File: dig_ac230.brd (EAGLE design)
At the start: 100 x 85 mm, 134 parts, among them IC1 74HC595D, IC101 ATMEGA32A-AU, IC102 DS1337S, IC103 MAX487CSA, IC104 74HC166D, IC2 LTV-356T, IC3 LTV-356T, IC4 LTV-356T, IC5 LTV-356T, IC6 LTV-356T, IC7 LTV-356T, IC8 LTV-356T, IC9 LTV-356T, K301 S202S02, K302 S202S02, K303 S202S02, K304 S202S02, K305 S202S02, K306 S202S02, K307 S202S02, K308 S202S02, Q1 32,768kHz, Q2 BCR191, Q3 BCR191, Q4 BCR191, Q5 BCR191, Q6 BCR191, Q7 BCR191, Q8 BCR191, Q9 BCR191, X1 RIA-73-02, X10 RIA-73-02, X11 RIA-73-02, X12 RIA-73-02, X2 RIA-73-02, X3 RIA-73-02, X4 RIA-73-02, X5 RIA-73-02, X6 RIA-73-02, X7 RIA-73-02, X8 RIA-73-02, X9 RIA-73-02

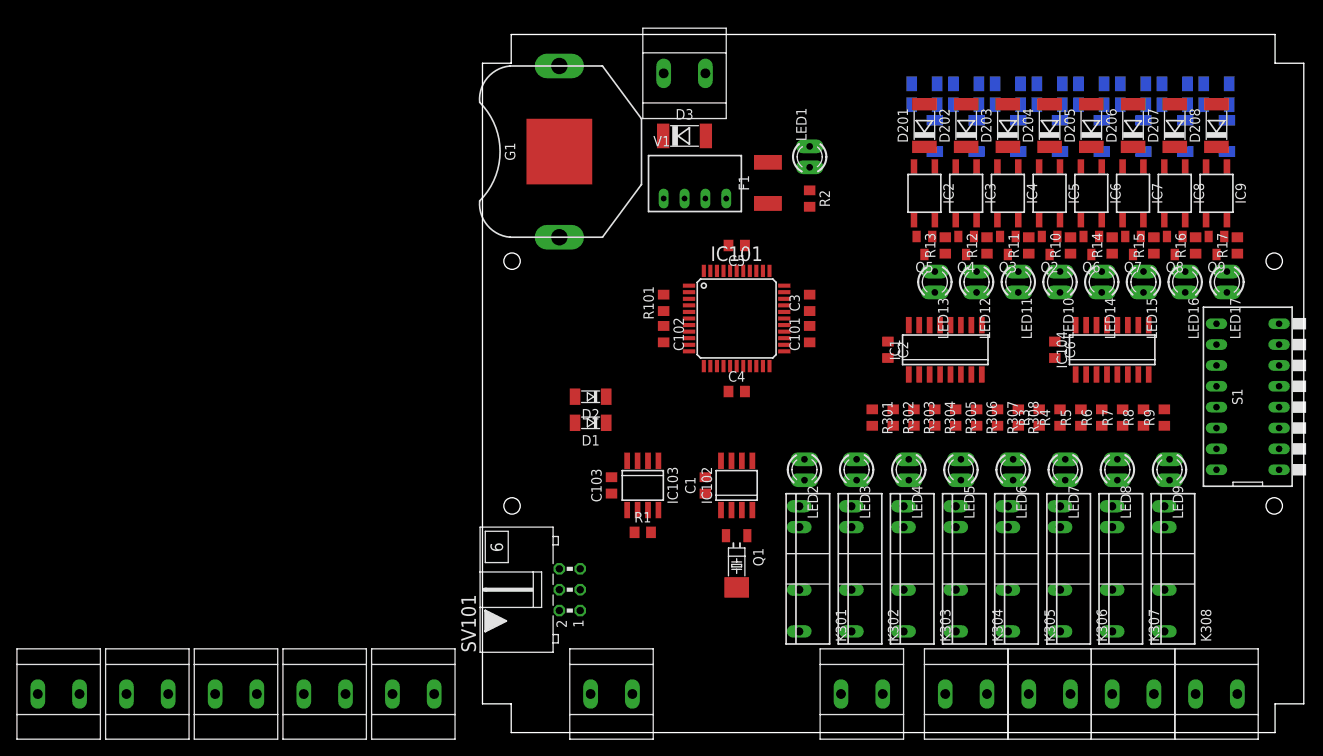
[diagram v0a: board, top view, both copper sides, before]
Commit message: Bauteile neu positoniert
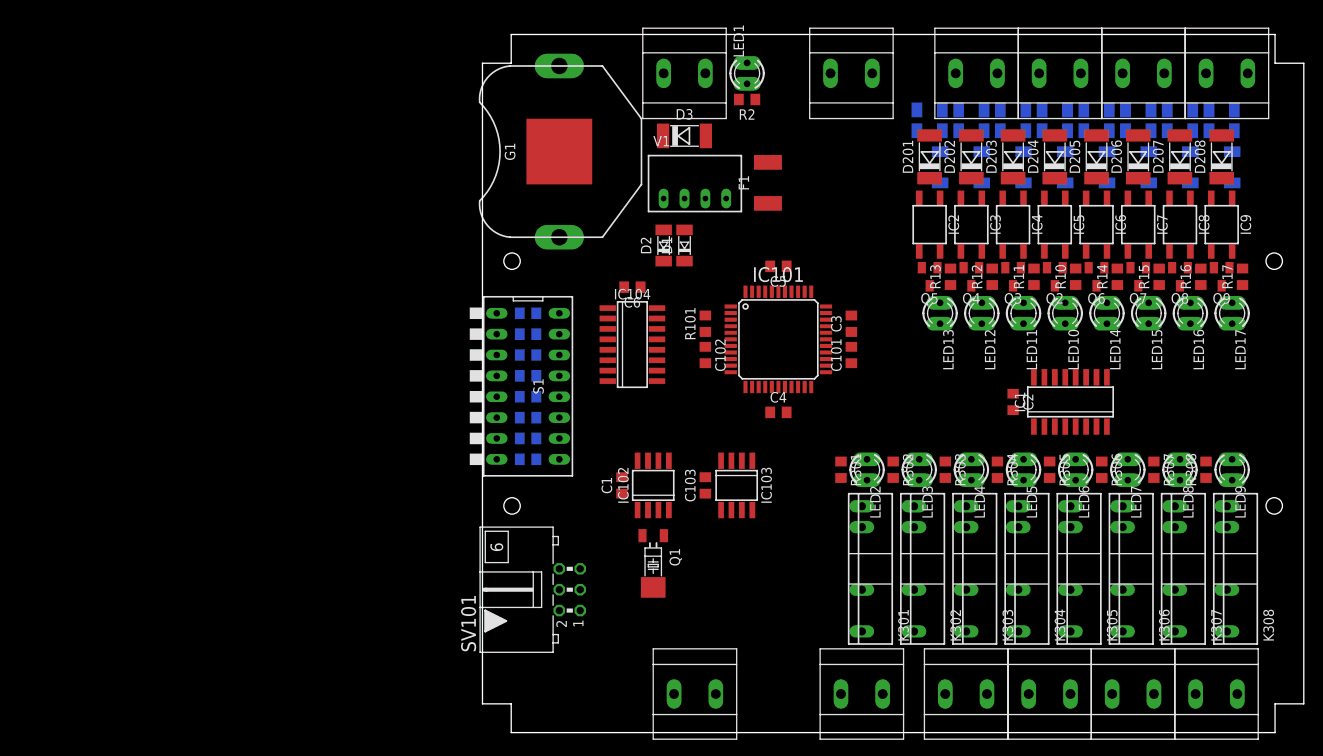
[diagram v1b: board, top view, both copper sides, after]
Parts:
- moved X6 151.6 mm to (92.7, 80.6), turned to 180 degrees
- moved X5 133.9 mm to (82.5, 80.6), turned to 180 degrees
- moved X7 122.6 mm to (47.0, 80.6), turned to 180 degrees
- moved X4 117.2 mm to (72.4, 80.6), turned to 180 degrees
- moved X3 102.0 mm to (62.2, 80.6), turned to 180 degrees
- moved S1 87.6 mm to (7.62, 42.5), turned to 270 degrees
- moved R9 77.5 mm to (7.62, 36.2), flipped to the bottom, turned to 180 degrees
- moved R8 74.9 mm to (7.62, 38.7), flipped to the bottom, turned to 180 degrees
- moved R7 72.4 mm to (7.62, 41.3), flipped to the bottom, turned to 180 degrees
- moved R6 70.0 mm to (7.62, 43.8), flipped to the bottom, turned to 180 degrees
- moved R5 67.7 mm to (7.62, 46.4), flipped to the bottom, turned to 180 degrees
- moved R4 65.6 mm to (7.62, 48.9), flipped to the bottom, turned to 180 degrees
- moved R3 63.5 mm to (7.62, 51.4), flipped to the bottom, turned to 180 degrees
- moved IC104 58.4 mm to (20.3, 47.6), turned to 270 degrees
- moved C6 52.0 mm to (20.3, 54.6), turned to 180 degrees
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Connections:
- net GNDIO renamed N
- net N$90 renamed L
- net +5V: now also S1.14, S1.24, S1.34, S1.44, S1.54, S1.64, S1.74; no longer S1.13, S1.23, S1.33, S1.43, S1.53, S1.63, S1.73
- net N$20: now also X2.1; no longer X2.2
- net N$22: now also X2.2; no longer X2.1
- net N$26: now also S1.13; no longer S1.14
- net N$27: now also S1.23; no longer S1.24
- net N$28: now also S1.33; no longer S1.34
- net N$29: now also S1.43; no longer S1.44
- net N$30: now also S1.53; no longer S1.54
- net N$31: now also S1.63; no longer S1.64
- net N$32: now also S1.73; no longer S1.74

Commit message: rev1 geroutet
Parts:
- moved IC103 11.4 mm to (21.6, 29.8)
- moved C103 11.4 mm to (17.8, 29.8), turned to 270 degrees
- moved C1 9.55 mm to (28.6, 29.8), turned to 270 degrees
- moved IC102 9.55 mm to (32.4, 29.8)
- moved Q1 9.55 mm to (32.4, 22.2)
- moved R101 5.85 mm to (24.8, 54.0)
- moved D1 4.84 mm to (31.1, 61.6), turned to 0 degrees
- moved C3 3.70 mm to (50.2, 48.3), turned to 270 degrees
- moved C102 2.69 mm to (27.3, 48.3)
- moved C101 2.01 mm to (46.4, 48.3)
- moved D2 2.01 mm to (24.8, 61.6), turned to 180 degrees
- moved C4 1.42 mm to (36.8, 38.7)
- moved C5 1.42 mm to (36.8, 57.8)
- moved IC101 1.27 mm to (36.8, 48.3)
- moved C6 1.27 mm to (19.1, 54.6)
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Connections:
- net N$20: now also S1.84; no longer R1.1
- net N$22: now also R1.1; no longer S1.84
- net RE: now also IC101.14; no longer IC101.13
- net TE: now also IC101.13; no longer IC101.14
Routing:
- net +5V: track 0.00 -> 278.5 mm, vias 0 -> 23
- net L: track 0.00 -> 133.7 mm
- net GND: track 0.00 -> 114.4 mm, vias 0 -> 18
- net C1: track 0.00 -> 79.3 mm, vias 0 -> 3
- net C2: track 0.00 -> 67.6 mm, vias 0 -> 4
- net !R: track 0.00 -> 67.0 mm, vias 0 -> 3
- net IN7: track 0.00 -> 65.6 mm, vias 0 -> 2
- net N: track 0.00 -> 64.7 mm
- net IN6: track 0.00 -> 60.2 mm, vias 0 -> 2
- net VCC: track 0.00 -> 58.6 mm, vias 0 -> 4
- net MISO: track 0.00 -> 56.8 mm, vias 0 -> 2
- net IN5: track 0.00 -> 54.8 mm, vias 0 -> 2
- net MOSI: track 0.00 -> 54.7 mm, vias 0 -> 2
- net SCK: track 0.00 -> 52.3 mm, vias 0 -> 2
- net N$42: track 0.00 -> 49.5 mm, vias 0 -> 2
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- added copper zone on layer 1, net +5V
- added copper zone on layer 16, net GND

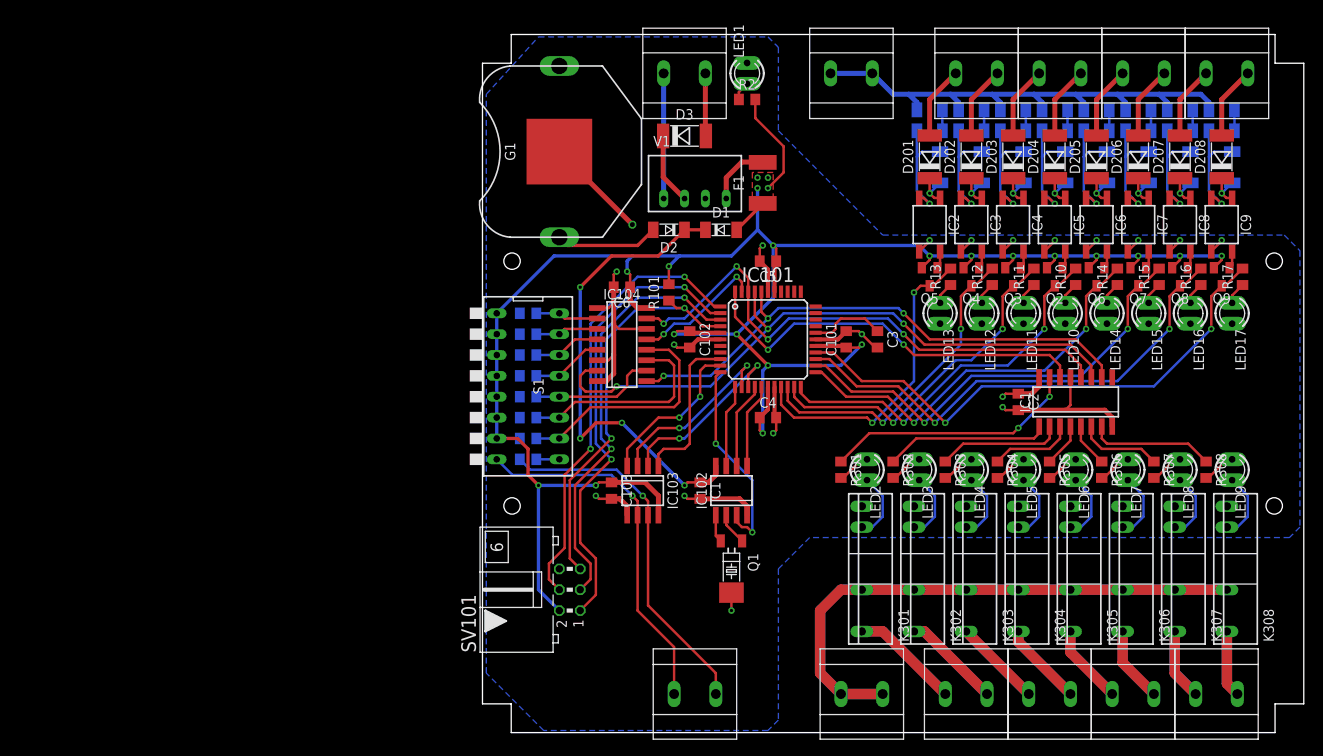
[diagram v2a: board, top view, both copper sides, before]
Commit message: kleinere Designfehler beseitigt
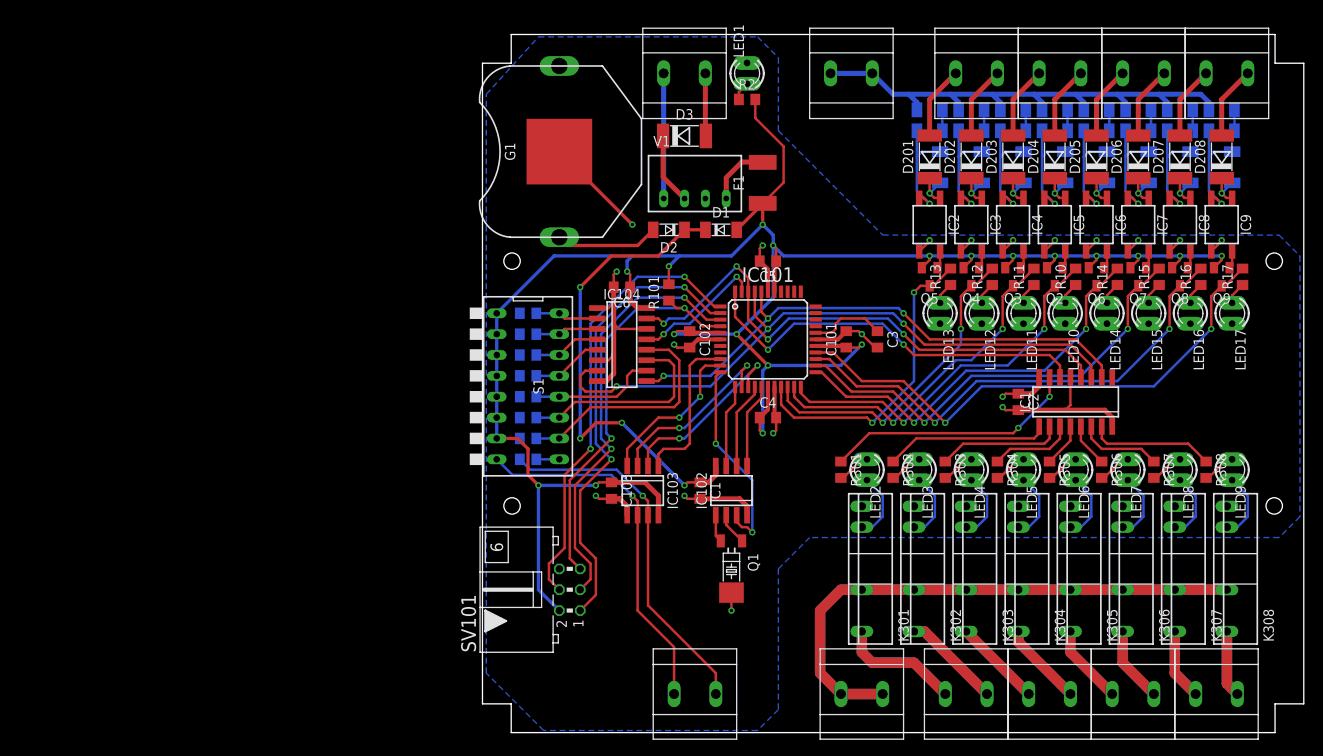
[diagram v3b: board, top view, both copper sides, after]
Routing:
- net N$68: track 26.6 -> 29.6 mm
- net +5V: track 278.5 -> 279.3 mm, vias 23 -> 20
- removed copper zone on layer 1, net +5V
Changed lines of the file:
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@@
 <hole x="5.6701" y="27.981" drill="2"/>
 <hole x="5.6701" y="57.781" drill="2"/>
-<polygon width="0" layer="40">
-<vertex x="2.0701" y="85.381"/>
-<vertex x="2.0701" y="0.381"/>
-<vertex x="8.0701" y="0.381"/>
-<vertex x="8.0701" y="85.381"/>
-</polygon>
-<polygon width="0" layer="40">
-<vertex x="96.0701" y="0.381"/>
-<vertex x="96.0701" y="85.381"/>
-<vertex x="102.0701" y="85.381"/>
-<vertex x="102.0701" y="0.381"/>
-</polygon>
-<polygon width="0" layer="40">
-<vertex x="2.0701" y="0.381"/>
-<vertex x="2.0701" y="3.381"/>
-<vertex x="101.4351" y="3.381"/>
-<vertex x="102.0701" y="0.381"/>
-</polygon>
-<polygon width="0" layer="40">
-<vertex x="2.0701" y="85.381"/>
-<vertex x="2.0701" y="82.381"/>
-<vertex x="102.0701" y="82.381"/>
-<vertex x="102.0701" y="85.381"/>
-</polygon>
-<polygon width="0" layer="39">
-<vertex x="4.0701" y="38.881"/>
-<vertex x="4.0701" y="46.881"/>
-<vertex x="2.0701" y="46.881"/>
-<vertex x="2.0701" y="38.881"/>
-</polygon>
-<polygon width="0" layer="39">
-<vertex x="102.0701" y="46.881"/>
-<vertex x="102.0701" y="38.881"/>
-<vertex x="100.0701" y="38.881"/>
-<vertex x="100.0701" y="46.881"/>
-</polygon>
 <circle x="8.8901" y="80.681" radius="1.8" width="0.1" layer="101"/>
 <circle x="13.9701" y="80.681" radius="1.8" width="0.1" layer="101"/>
@@
 <polygon width="0.4064" layer="16">
 <vertex x="8.89" y="85.09"/>
-<vertex x="36.83" y="85.09"/>
-<vertex x="38.1" y="83.82"/>
+<vertex x="35.56" y="85.09"/>
+<vertex x="38.1" y="82.55"/>
 <vertex x="38.1" y="73.66"/>
 <vertex x="50.8" y="60.96"/>
-<vertex x="99.695" y="60.96"/>
-<vertex x="101.6" y="59.055"/>
-<vertex x="101.6" y="25.4"/>
-<vertex x="100.33" y="24.13"/>
+<vertex x="99.06" y="60.96"/>
+<vertex x="101.6" y="58.42"/>
+<vertex x="101.6" y="26.67"/>
+<vertex x="99.06" y="24.13"/>
 <vertex x="41.91" y="24.13"/>
 <vertex x="38.1" y="20.32"/>
-<vertex x="38.1" y="1.905"/>
-<vertex x="36.83" y="0.635"/>
+<vertex x="38.1" y="3.175"/>
+<vertex x="35.56" y="0.635"/>
 <vertex x="9.525" y="0.635"/>
 <vertex x="2.54" y="7.62"/>
@@
 <wire x1="16.05" y1="45.72" x2="17.415" y2="45.72" width="0.3048" layer="1"/>
 <wire x1="17.415" y1="45.72" x2="18.05" y2="46.355" width="0.3048" layer="1"/>
-<wire x1="11.43" y1="71.12" x2="20.32" y2="62.23" width="0.6096" layer="1"/>
-<via x="20.32" y="62.23" extent="1-16" drill="0.6"/>
+<wire x1="11.43" y1="71.12" x2="20.32" y2="62.23" width="0.4064" layer="1"/>
+<via x="20.32" y="62.23" extent="1-16" drill="0.4"/>
 <wire x1="42.63" y1="48.26" x2="45.355" y2="48.26" width="0.508" layer="1"/>
 <wire x1="45.355" y1="48.26" x2="46.355" y2="49.26" width="0.508" layer="1"/>
@@
 <wire x1="21.86" y1="30.845" x2="23.495" y2="29.21" width="0.6096" layer="1"/>
 <via x="19.685" y="56.515" extent="1-16" drill="0.4"/>
-<polygon width="0.6096" layer="1">
-<vertex x="37.465" y="64.135"/>
-<vertex x="37.465" y="68.58"/>
-<vertex x="34.925" y="68.58"/>
-<vertex x="34.925" y="64.135"/>
-</polygon>
-<via x="36.83" y="66.675" extent="1-16" drill="0.4"/>
-<via x="35.56" y="66.675" extent="1-16" drill="0.4"/>
-<via x="36.83" y="67.945" extent="1-16" drill="0.4"/>
+<via x="36.195" y="62.23" extent="1-16" drill="0.4"/>
 <wire x1="20.05" y1="54.61" x2="20.05" y2="52.975" width="0.6096" layer="1"/>
 <wire x1="20.05" y1="52.975" x2="20.955" y2="52.07" width="0.6096" layer="1"/>
 <wire x1="20.955" y1="52.07" x2="22.05" y2="52.07" width="0.6096" layer="1"/>
-<via x="35.56" y="67.945" extent="1-16" drill="0.4"/>
 <wire x1="33.015" y1="61.595" x2="33.015" y2="61.63" width="0.6096" layer="1"/>
 <wire x1="35.29" y1="77.47" x2="35.29" y2="75.2" width="0.3048" layer="1"/>
 <wire x1="35.29" y1="75.2" x2="38.735" y2="71.755" width="0.3048" layer="1"/>
-<wire x1="38.735" y1="71.755" x2="38.735" y2="68.58" width="0.3048" layer="1"/>
-<wire x1="38.735" y1="68.58" x2="36.83" y2="66.675" width="0.3048" layer="1"/>
+<wire x1="38.735" y1="71.755" x2="38.735" y2="67.35" width="0.3048" layer="1"/>
 <wire x1="42.63" y1="47.46" x2="46.155" y2="47.46" width="0.508" layer="1"/>
 <wire x1="46.155" y1="47.46" x2="46.355" y2="47.26" width="0.508" layer="1"/>
@@
 <wire x1="3.81" y1="41.275" x2="3.81" y2="38.735" width="0.4064" layer="16"/>
 <wire x1="3.81" y1="38.735" x2="3.81" y2="36.195" width="0.4064" layer="16"/>
-<wire x1="35.56" y1="66.675" x2="35.56" y2="61.595" width="0.4064" layer="16"/>
-<wire x1="35.56" y1="61.595" x2="37.465" y2="59.69" width="0.4064" layer="16"/>
-<wire x1="35.56" y1="61.595" x2="32.385" y2="58.42" width="0.4064" layer="16"/>
+<wire x1="36.195" y1="62.23" x2="32.385" y2="58.42" width="0.4064" layer="16"/>
 <wire x1="32.385" y1="58.42" x2="26.035" y2="58.42" width="0.4064" layer="16"/>
 <wire x1="26.035" y1="58.42" x2="20.32" y2="58.42" width="0.4064" layer="16"/>
@@
 <via x="24.765" y="57.15" extent="1-16" drill="0.4"/>
 <wire x1="24.765" y1="57.15" x2="26.035" y2="58.42" width="0.4064" layer="16"/>
-<wire x1="37.465" y1="59.69" x2="55.245" y2="59.69" width="0.4064" layer="16"/>
-<wire x1="55.245" y1="59.69" x2="56.515" y2="58.42" width="0.4064" layer="16"/>
 <wire x1="37.465" y1="59.69" x2="37.465" y2="53.34" width="0.4064" layer="16"/>
 <wire x1="37.465" y1="53.34" x2="33.02" y2="48.895" width="0.4064" layer="16"/>
@@
 <wire x1="8.89" y1="17.78" x2="8.89" y2="30.48" width="0.4064" layer="16"/>
 <wire x1="36.195" y1="64.775" x2="33.015" y2="61.595" width="0.4064" layer="1"/>
-<wire x1="70.805" y1="56.98" x2="69.85" y2="43.64" width="0" layer="19" extent="1-1"/>
+<wire x1="37.465" y1="59.69" x2="37.465" y2="60.96" width="0.4064" layer="16"/>
+<wire x1="37.465" y1="60.96" x2="36.195" y2="62.23" width="0.4064" layer="16"/>
+<wire x1="56.515" y1="58.42" x2="38.735" y2="58.42" width="0.4064" layer="16"/>
+<wire x1="38.735" y1="58.42" x2="37.465" y2="59.69" width="0.4064" layer="16"/>
+<wire x1="69.85" y1="43.64" x2="70.805" y2="56.98" width="0" layer="19" extent="1-1"/>
+<wire x1="38.735" y1="67.35" x2="36.195" y2="64.81" width="0.3048" layer="1"/>
+<wire x1="36.195" y1="64.775" x2="36.195" y2="62.23" width="0.4064" layer="1"/>
 </signal>
 <signal name="N$42">
@@
 <contactref element="X8" pad="1"/>
 <contactref element="K301" pad="1"/>
-<wire x1="48.26" y1="12.7" x2="50.8" y2="12.7" width="1.27" layer="16"/>
-<wire x1="50.8" y1="12.7" x2="58.42" y2="5.08" width="1.27" layer="16"/>
-<wire x1="48.26" y1="12.7" x2="50.8" y2="12.7" width="1.27" layer="1"/>
-<wire x1="50.8" y1="12.7" x2="58.42" y2="5.08" width="1.27" layer="1"/>
+<wire x1="48.26" y1="12.7" x2="48.26" y2="10.16" width="1.27" layer="1"/>
+<wire x1="48.26" y1="10.16" x2="49.53" y2="8.89" width="1.27" layer="1"/>
+<wire x1="49.53" y1="8.89" x2="54.61" y2="8.89" width="1.27" layer="1"/>
+<wire x1="54.61" y1="8.89" x2="58.42" y2="5.08" width="1.27" layer="1"/>
+<wire x1="48.26" y1="12.7" x2="48.26" y2="10.16" width="1.27" layer="16"/>
+<wire x1="48.26" y1="10.16" x2="49.53" y2="8.89" width="1.27" layer="16"/>
+<wire x1="49.53" y1="8.89" x2="54.61" y2="8.89" width="1.27" layer="16"/>
+<wire x1="54.61" y1="8.89" x2="58.42" y2="5.08" width="1.27" layer="16"/>
 </signal>
 <signal name="N$72">
